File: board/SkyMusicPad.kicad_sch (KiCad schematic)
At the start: 32 parts, among them SW1 RotaryEncoder_Switch

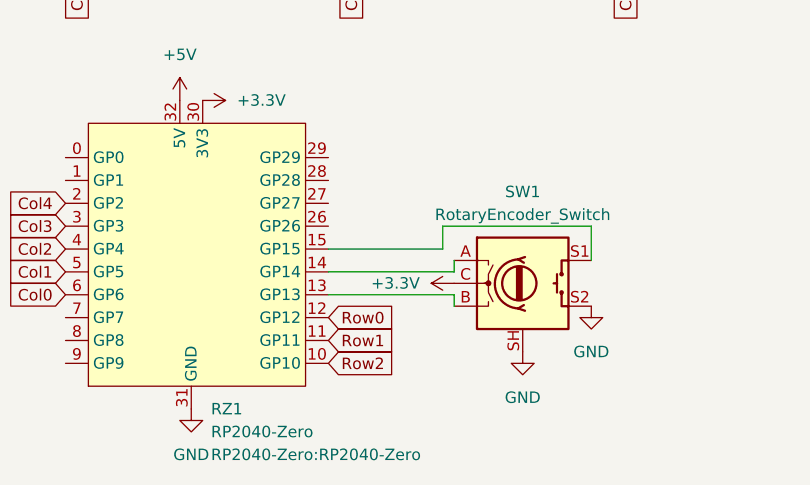
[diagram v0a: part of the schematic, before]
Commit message: Adjusted rotary encoder to have common point GND
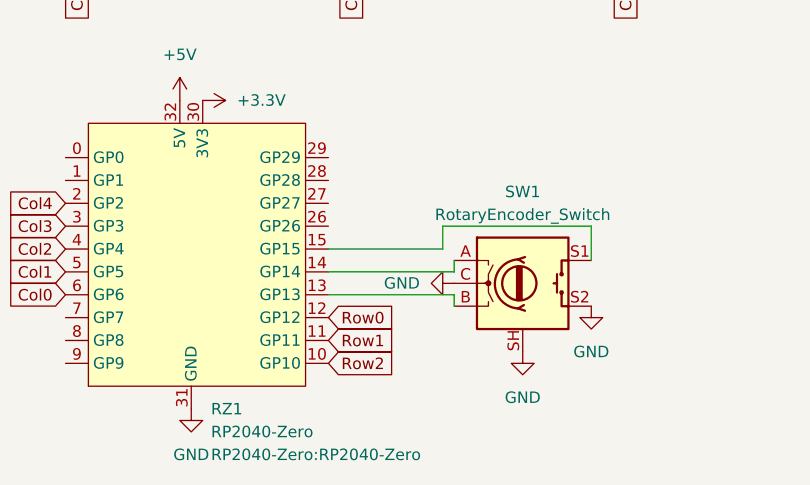
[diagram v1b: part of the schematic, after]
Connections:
- net +3.3V: no longer SW1.C
- net GND: now also SW1.C
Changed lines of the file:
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@@
+    )
+  )
+  (symbol (lib_id "power:GND") (at 191.77 120.65 270) (unit 1)
+    (in_bom yes) (on_board yes) (dnp no) (fields_autoplaced)
+    (property "Reference" "#PWR04" (at 185.42 120.65 0)
+      (effects (font (size 1.27 1.27)) hide)
+    )
+    (property "Value" "GND" (at 187.96 120.65 90)
+      (effects (font (size 1.27 1.27)) (justify right))
+    )
+    (property "Footprint" "" (at 191.77 120.65 0)
+      (effects (font (size 1.27 1.27)) hide)
+    )
+    (property "Datasheet" "" (at 191.77 120.65 0)
+      (effects (font (size 1.27 1.27)) hide)
+    )
+    (pin "1")
+    (instances
+      (project "SkyMusicPad"
+        (path "/892c3dfc-ea33-45ad-8367-abbb3e31e120"
+          (reference "#PWR04") (unit 1)
+        )
+      )
     )
   )
@@
         )
       )
-    )
-  )
-  (symbol (lib_id "power:+3.3V") (at 191.77 120.65 90) (unit 1)
-    (in_bom yes) (on_board yes) (dnp no) (fields_autoplaced)
-    (property "Reference" "#PWR04" (at 195.58 120.65 0)
-      (effects (font (size 1.27 1.27)) hide)
-    )
-    (property "Value" "+3.3V" (at 187.96 120.65 90)
-      (effects (font (size 1.27 1.27)) (justify left))
-    )
-    (property "Footprint" "" (at 191.77 120.65 0)
-      (effects (font (size 1.27 1.27)) hide)
-    )
-    (property "Datasheet" "" (at 191.77 120.65 0)
-      (effects (font (size 1.27 1.27)) hide)
-    )
-    (pin "1")
-    (instances
-      (project "SkyMusicPad"
-        (path "/892c3dfc-ea33-45ad-8367-abbb3e31e120"
-          (reference "#PWR04") (unit 1)
-        )
-      )

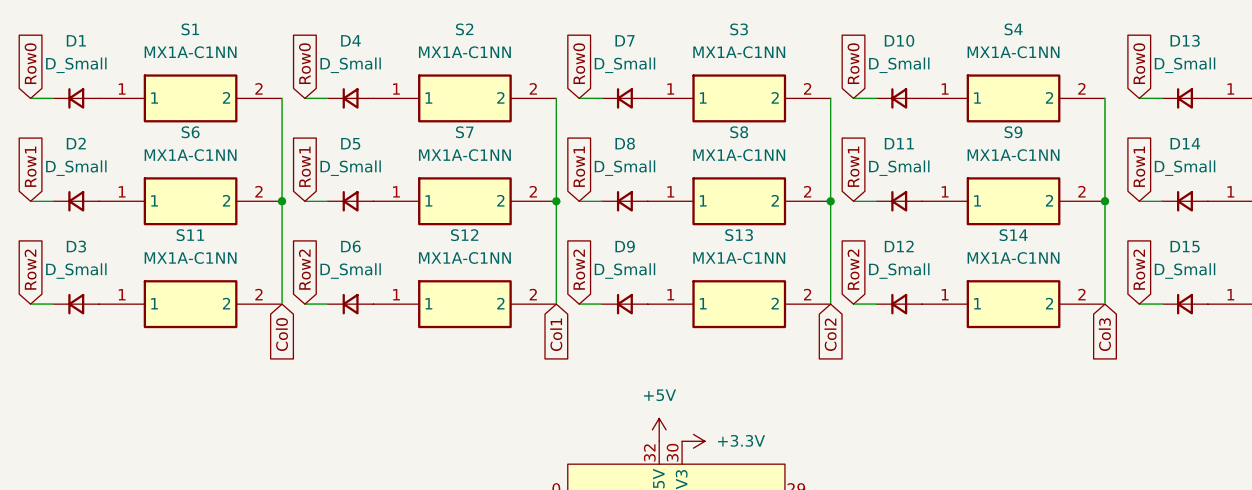
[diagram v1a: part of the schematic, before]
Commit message: Fixed the use of the incorrect footprint for MX
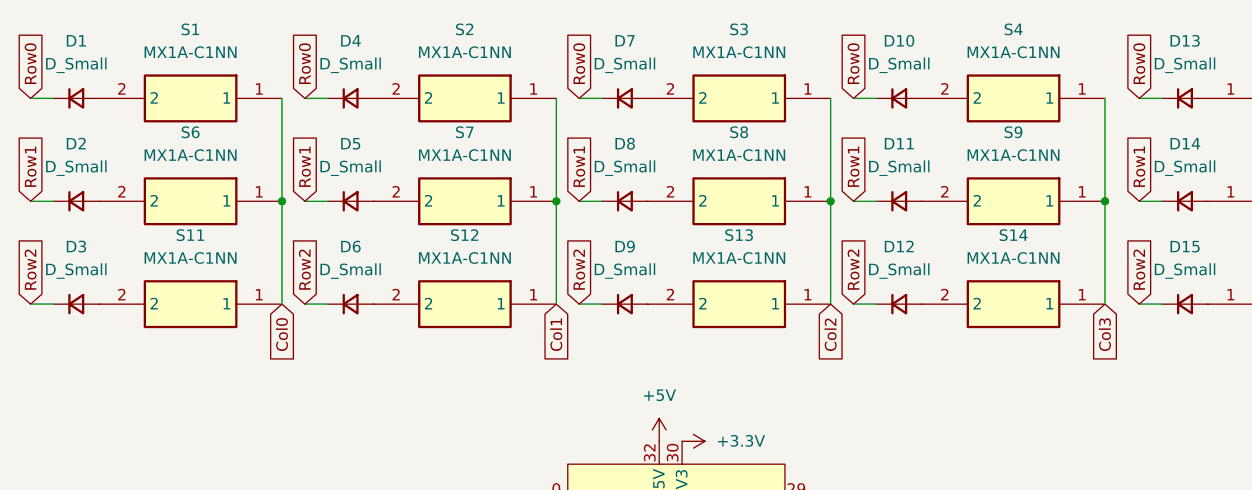
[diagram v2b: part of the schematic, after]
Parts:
- S1, S10, S11, S12, S13, S14, S15, S2, S3, S4, S5, S6, S7, S8, S9: footprint MX1A-C1NN:MX1AC1NN -> Button_Switch_Keyboard:SW_Cherry_MX_1.00u_PCB
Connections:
- net Col0: now also S1.1, S11.1, S6.1; no longer S1.2, S11.2, S6.2
- net Col1: now also S12.1, S2.1, S7.1; no longer S12.2, S2.2, S7.2
- net Col2: now also S13.1, S3.1, S8.1; no longer S13.2, S3.2, S8.2
- net Col3: now also S14.1, S4.1, S9.1; no longer S14.2, S4.2, S9.2
- net at D6.2 (A): now also S12.2; no longer S12.1
- net at D12.2 (A): now also S14.2; no longer S14.1
- net at D9.2 (A): now also S13.2; no longer S13.1
- net at D2.2 (A): now also S6.2; no longer S6.1
- net at D1.2 (A): now also S1.2; no longer S1.1
- net at D3.2 (A): now also S11.2; no longer S11.1
- net at D11.2 (A): now also S9.2; no longer S9.1
- net at D4.2 (A): now also S2.2; no longer S2.1
- net at D8.2 (A): now also S8.2; no longer S8.1
- net at D10.2 (A): now also S4.2; no longer S4.1
- net at D7.2 (A): now also S3.2; no longer S3.1
- net at D5.2 (A): now also S7.2; no longer S7.1

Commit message: a
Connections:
- net Col4: now also S10.1, S15.1, S5.1; no longer S10.2, S15.2, S5.2
- net at D14.2 (A): now also S10.2; no longer S10.1
- net at D15.2 (A): now also S15.2; no longer S15.1
- net at D13.2 (A): now also S5.2; no longer S5.1
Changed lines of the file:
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@@
 (kicad_sch (version 20230121) (generator eeschema)
   (paper "A4")
+  (junction (at 242.57 73.66) (diameter 0) (color 0 0 0 0)
+  )
   (junction (at 149.86 73.66) (diameter 0) (color 0 0 0 0)
   )
-  (junction (at 242.57 73.66) (diameter 0) (color 0 0 0 0)
-  )
   (junction (at 210.82 73.66) (diameter 0) (color 0 0 0 0)
   )
@@
     (stroke (width 0) (type default))
   )
+  (wire (pts (xy 152.4 85.09) (xy 154.94 85.09))
+    (stroke (width 0) (type default))
+  )
   (wire (pts (xy 242.57 73.66) (xy 242.57 85.09))
-    (stroke (width 0) (type default))
-  )
-  (wire (pts (xy 152.4 85.09) (xy 154.94 85.09))
     (stroke (width 0) (type default))
   )
@@
     )
   )
-  (symbol (lib_id "MX1A-C1NN:MX1A-C1NN") (at 222.25 62.23 0) (unit 1)
-    (in_bom yes) (on_board yes) (dnp no) (fields_autoplaced)
+  (symbol (lib_id "MX1A-C1NN:MX1A-C1NN") (at 242.57 62.23 0) (mirror y) (unit 1)
+    (in_bom yes) (on_board yes) (dnp no)
     (property "Reference" "S5" (at 232.41 54.61 0)
       (effects (font (size 1.27 1.27)))
@@
       (effects (font (size 1.27 1.27)))
     )
-    (property "Footprint" "Button_Switch_Keyboard:SW_Cherry_MX_1.00u_PCB" (at 238.76 157.15 0)
-      (effects (font (size 1.27 1.27)) (justify left top) hide)
-    )
-    (property "Datasheet" "https://media.digikey.com/pdf/Data%20Sheets/Cherry%20PDFs/MX%20Series.pdf" (at 238.76 257.15 0)
-      (effects (font (size 1.27 1.27)) (justify left top) hide)
-    )
-    (property "Height" "15.2" (at 238.76 457.15 0)
-      (effects (font (size 1.27 1.27)) (justify left top) hide)
-    )
-    (property "Mouser Part Number" "540-MX1A-C1NN" (at 238.76 557.15 0)
-      (effects (font (size 1.27 1.27)) (justify left top) hide)
-    )
-    (property "Mouser Price/Stock" "https://www.mouser.co.uk/ProductDetail/CHERRY/MX1A-C1NN?qs=Z9t1pRjfOcwvorA009Lo0w%3D%3D" (at 238.76 657.15 0)
-      (effects (font (size 1.27 1.27)) (justify left top) hide)
-    )
-    (property "Manufacturer_Name" "Cherry" (at 238.76 757.15 0)
-      (effects (font (size 1.27 1.27)) (justify left top) hide)
-    )
-    (property "Manufacturer_Part_Number" "MX1A-C1NN" (at 238.76 857.15 0)
+    (property "Footprint" "Button_Switch_Keyboard:SW_Cherry_MX_1.00u_PCB" (at 226.06 157.15 0)
+      (effects (font (size 1.27 1.27)) (justify left top) hide)
+    )
+    (property "Datasheet" "https://media.digikey.com/pdf/Data%20Sheets/Cherry%20PDFs/MX%20Series.pdf" (at 226.06 257.15 0)
+      (effects (font (size 1.27 1.27)) (justify left top) hide)
+    )
+    (property "Height" "15.2" (at 226.06 457.15 0)
+      (effects (font (size 1.27 1.27)) (justify left top) hide)
+    )
+    (property "Mouser Part Number" "540-MX1A-C1NN" (at 226.06 557.15 0)
+      (effects (font (size 1.27 1.27)) (justify left top) hide)
+    )
+    (property "Mouser Price/Stock" "https://www.mouser.co.uk/ProductDetail/CHERRY/MX1A-C1NN?qs=Z9t1pRjfOcwvorA009Lo0w%3D%3D" (at 226.06 657.15 0)
+      (effects (font (size 1.27 1.27)) (justify left top) hide)
+    )
+    (property "Manufacturer_Name" "Cherry" (at 226.06 757.15 0)
+      (effects (font (size 1.27 1.27)) (justify left top) hide)
+    )
+    (property "Manufacturer_Part_Number" "MX1A-C1NN" (at 226.06 857.15 0)
       (effects (font (size 1.27 1.27)) (justify left top) hide)
     )
@@
     )
   )
-  (symbol (lib_id "MX1A-C1NN:MX1A-C1NN") (at 222.25 73.66 0) (unit 1)
-    (in_bom yes) (on_board yes) (dnp no) (fields_autoplaced)
+  (symbol (lib_id "MX1A-C1NN:MX1A-C1NN") (at 242.57 73.66 0) (mirror y) (unit 1)
+    (in_bom yes) (on_board yes) (dnp no)
     (property "Reference" "S10" (at 232.41 66.04 0)
       (effects (font (size 1.27 1.27)))
@@
       (effects (font (size 1.27 1.27)))
     )
-    (property "Footprint" "Button_Switch_Keyboard:SW_Cherry_MX_1.00u_PCB" (at 238.76 168.58 0)
-      (effects (font (size 1.27 1.27)) (justify left top) hide)
-    )
-    (property "Datasheet" "https://media.digikey.com/pdf/Data%20Sheets/Cherry%20PDFs/MX%20Series.pdf" (at 238.76 268.58 0)
-      (effects (font (size 1.27 1.27)) (justify left top) hide)
-    )
-    (property "Height" "15.2" (at 238.76 468.58 0)
-      (effects (font (size 1.27 1.27)) (justify left top) hide)
-    )
-    (property "Mouser Part Number" "540-MX1A-C1NN" (at 238.76 568.58 0)
-      (effects (font (size 1.27 1.27)) (justify left top) hide)
-    )
-    (property "Mouser Price/Stock" "https://www.mouser.co.uk/ProductDetail/CHERRY/MX1A-C1NN?qs=Z9t1pRjfOcwvorA009Lo0w%3D%3D" (at 238.76 668.58 0)
-      (effects (font (size 1.27 1.27)) (justify left top) hide)
-    )
-    (property "Manufacturer_Name" "Cherry" (at 238.76 768.58 0)
-      (effects (font (size 1.27 1.27)) (justify left top) hide)
-    )
-    (property "Manufacturer_Part_Number" "MX1A-C1NN" (at 238.76 868.58 0)
+    (property "Footprint" "Button_Switch_Keyboard:SW_Cherry_MX_1.00u_PCB" (at 226.06 168.58 0)
+      (effects (font (size 1.27 1.27)) (justify left top) hide)
+    )
+    (property "Datasheet" "https://media.digikey.com/pdf/Data%20Sheets/Cherry%20PDFs/MX%20Series.pdf" (at 226.06 268.58 0)
+      (effects (font (size 1.27 1.27)) (justify left top) hide)
+    )
+    (property "Height" "15.2" (at 226.06 468.58 0)
+      (effects (font (size 1.27 1.27)) (justify left top) hide)
+    )
+    (property "Mouser Part Number" "540-MX1A-C1NN" (at 226.06 568.58 0)
+      (effects (font (size 1.27 1.27)) (justify left top) hide)
+    )
+    (property "Mouser Price/Stock" "https://www.mouser.co.uk/ProductDetail/CHERRY/MX1A-C1NN?qs=Z9t1pRjfOcwvorA009Lo0w%3D%3D" (at 226.06 668.58 0)
+      (effects (font (size 1.27 1.27)) (justify left top) hide)
+    )
+    (property "Manufacturer_Name" "Cherry" (at 226.06 768.58 0)
+      (effects (font (size 1.27 1.27)) (justify left top) hide)
+    )
+    (property "Manufacturer_Part_Number" "MX1A-C1NN" (at 226.06 868.58 0)
       (effects (font (size 1.27 1.27)) (justify left top) hide)
     )
@@
     )
   )
-  (symbol (lib_id "MX1A-C1NN:MX1A-C1NN") (at 222.25 85.09 0) (unit 1)
-    (in_bom yes) (on_board yes) (dnp no) (fields_autoplaced)
+  (symbol (lib_id "MX1A-C1NN:MX1A-C1NN") (at 242.57 85.09 0) (mirror y) (unit 1)
+    (in_bom yes) (on_board yes) (dnp no)
     (property "Reference" "S15" (at 232.41 77.47 0)
       (effects (font (size 1.27 1.27)))
@@
       (effects (font (size 1.27 1.27)))
     )
-    (property "Footprint" "Button_Switch_Keyboard:SW_Cherry_MX_1.00u_PCB" (at 238.76 180.01 0)
-      (effects (font (size 1.27 1.27)) (justify left top) hide)
-    )
-    (property "Datasheet" "https://media.digikey.com/pdf/Data%20Sheets/Cherry%20PDFs/MX%20Series.pdf" (at 238.76 280.01 0)
-      (effects (font (size 1.27 1.27)) (justify left top) hide)
-    )
-    (property "Height" "15.2" (at 238.76 480.01 0)
-      (effects (font (size 1.27 1.27)) (justify left top) hide)
-    )
-    (property "Mouser Part Number" "540-MX1A-C1NN" (at 238.76 580.01 0)
-      (effects (font (size 1.27 1.27)) (justify left top) hide)
-    )
-    (property "Mouser Price/Stock" "https://www.mouser.co.uk/ProductDetail/CHERRY/MX1A-C1NN?qs=Z9t1pRjfOcwvorA009Lo0w%3D%3D" (at 238.76 680.01 0)
-      (effects (font (size 1.27 1.27)) (justify left top) hide)
-    )
-    (property "Manufacturer_Name" "Cherry" (at 238.76 780.01 0)
-      (effects (font (size 1.27 1.27)) (justify left top) hide)
-    )
-    (property "Manufacturer_Part_Number" "MX1A-C1NN" (at 238.76 880.01 0)
-      (effects (font (size 1.27 1.27)) (justify left top) hide)
-    )
+    (property "Footprint" "Button_Switch_Keyboard:SW_Cherry_MX_1.00u_PCB" (at 226.06 180.01 0)
+      (effects (font (size 1.27 1.27)) (justify left top) hide)
+    )
+    (property "Datasheet" "https://media.digikey.com/pdf/Data%20Sheets/Cherry%20PDFs/MX%20Series.pdf" (at 226.06 280.01 0)
+      (effects (font (size 1.27 1.27)) (justify left top) hide)
+    )
+    (property "Height" "15.2" (at 226.06 480.01 0)
+      (effects (font (size 1.27 1.27)) (justify left top) hide)
+    )
+    (property "Mouser Part Number" "540-MX1A-C1NN" (at 226.06 580.01 0)
+      (effects (font (size 1.27 1.27)) (justify left top) hide)
+    )
+    (property "Mouser Price/Stock" "https://www.mouser.co.uk/ProductDetail/CHERRY/MX1A-C1NN?qs=Z9t1pRjfOcwvorA009Lo0w%3D%3D" (at 226.06 680.01 0)
+      (effects (font (size 1.27 1.27)) (justify left top) hide)
+    )
+    (property "Manufacturer_Name" "Cherry" (at 226.06 780.01 0)
+      (effects (font (size 1.27 1.27)) (justify left top) hide)
+    )
+    (property "Manufacturer_Part_Number" "MX1A-C1NN" (at 226.06 880.01 0)
+      (effects (font (size 1.27 1.27)) (justify left top) hide)
+    )

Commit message: misc changes
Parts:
- removed RZ1: RP2040-Zero, RP2040-Zero:RP2040-Zero, symbol rp2040-zero:RP2040-Zero
- added C1, C10, C11, C12, C2, C4, C6, C7, C8, C9: 100n, Capacitor_SMD:C_0402_1005Metric, symbol Device:C
- added C13, C14: 27p, Capacitor_SMD:C_0402_1005Metric, symbol Device:C
- added C15, C16, C17: 10u, Capacitor_SMD:C_0805_2012Metric, symbol Device:C
- added C3, C5: 1u, Capacitor_SMD:C_0402_1005Metric, symbol Device:C
- added J1: USB_C_Receptacle_USB2.0, Connector_USB:USB_C_Receptacle_Amphenol_12401548E4-2A, symbol Connector:USB_C_Receptacle_USB2.0
- added R1, R2: 27, Capacitor_SMD:C_0402_1005Metric, symbol Device:R
- added R3, R5: 1k, Capacitor_SMD:C_0402_1005Metric, symbol Device:R
- added R4: DNF, Capacitor_SMD:C_0402_1005Metric, symbol Device:R
- added R6, R7: 5.1k, Capacitor_SMD:C_0402_1005Metric, symbol Device:R
- added SW2: SW_Push, symbol Switch:SW_Push
- added U1: RP2040, Package_DFN_QFN:QFN-56-1EP_7x7mm_P0.4mm_EP3.2x3.2mm, symbol MCU_RaspberryPi:RP2040
- added U2: W25Q128JVS, Package_SO:SOIC-8_5.23x5.23mm_P1.27mm, symbol Memory_Flash:W25Q128JVS
- added U3: NCP1117-3.3_SOT223, Package_TO_SOT_SMD:SOT-223-3_TabPin2, symbol Regulator_Linear:NCP1117-3.3_SOT223
- added Y1: ABLS-12.000MHZ-B4-T, RP2040_minimal:Crystal_SMD_HC49-US, symbol Device:Crystal
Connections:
- net +3.3V: now also C10.1, C11.1, C12.1, C15.1, C17.1, C4.1, C5.1, C6.1, C7.1, C8.1, C9.1, R4.1, U1.1 (IOVDD), U1.10 (IOVDD), U1.22 (IOVDD), U1.33 (IOVDD), U1.42 (IOVDD), U1.43 (ADC_AVDD), U1.44 (VREG_IN), U1.48 (USB_VDD), U1.49 (IOVDD), U2.8 (VCC), U3.2 (VO)
- net +5V: now also C16.1, J1.A4 (VBUS), J1.A9 (VBUS), J1.B4 (VBUS), J1.B9 (VBUS), U3.3 (VI)
- net Col0: now also U1.8 (GPIO6)
- net Col1: now also U1.7 (GPIO5)
- net Col2: now also U1.6 (GPIO4)
- net Col3: now also U1.5 (GPIO3)
- net Col4: now also U1.4 (GPIO2)
- net GND: now also C1.2, C10.2, C11.2, C12.2, C13.2, C14.2, C15.2, C16.2, C17.2, C2.2, C3.2, C4.2, C5.2, C6.2, C7.2, C8.2, C9.2, J1.A1 (GND), J1.A12 (GND), J1.B1 (GND), J1.B12 (GND), J1.S1 (SHIELD), R6.1, R7.1, SW2.1, U1.19 (TESTEN), U1.57 (GND), U2.4 (GND), U3.1 (GND)
- net Row0: now also U1.18 (GPIO15)
- net Row1: now also U1.17 (GPIO14)
- net Row2: now also U1.16 (GPIO13)
- net GPIO18: now reaches SW1.A
- net GPIO18: now also U1.29 (GPIO18)
- net GPIO20: now reaches SW1.B
- net GPIO20: now also U1.31 (GPIO20)
- net GPIO16: now reaches SW1.S1
- net GPIO16: now also U1.27 (GPIO16)
- new net: J1.B5 (CC2), R7.2
- new net: J1.A5 (CC1), R6.2
- new net: C14.1, R5.2, Y1.2
- new net +1V1: C1.1, C2.1, C3.1, U1.23 (DVDD), U1.45 (VREG_VOUT), U1.50 (DVDD)
- new net GPIO0: U1.2 (GPIO0)
- new net GPIO1: U1.3 (GPIO1)
- new net GPIO10: U1.13 (GPIO10)
- new net GPIO11: U1.14 (GPIO11)
- new net GPIO12: U1.15 (GPIO12)
- new net GPIO17: U1.28 (GPIO17)
- new net GPIO19: U1.30 (GPIO19)
- new net GPIO21: U1.32 (GPIO21)
- new net GPIO22: U1.34 (GPIO22)
- new net GPIO23: U1.35 (GPIO23)
- new net GPIO24: U1.36 (GPIO24)
- new net GPIO25: U1.37 (GPIO25)
- new net GPIO26_ADC0: U1.38 (GPIO26_ADC0)
- new net GPIO27_ADC1: U1.39 (GPIO27_ADC1)
- new net GPIO28_ADC2: U1.40 (GPIO28_ADC2)
- new net GPIO29_ADC3: U1.41 (GPIO29_ADC3)
- new net GPIO7: U1.9 (GPIO7)
- new net GPIO8: U1.11 (GPIO8)
- new net GPIO9: U1.12 (GPIO9)
- new net PICO_USB_D+: R1.2, U1.47 (USB_DP)
- new net PICO_USB_D-: R2.2, U1.46 (USB_DM)
- new net QSPI_SCLK: U1.52 (QSPI_SCLK), U2.6 (CLK)
- new net QSPI_SD0: U1.53 (QSPI_SD0), U2.5 (DI(IO0))
- new net QSPI_SD1: U1.55 (QSPI_SD1), U2.2 (DO(IO1))
- new net QSPI_SD2: U1.54 (QSPI_SD2), U2.3 (IO2)
- new net QSPI_SD3: U1.51 (QSPI_SD3), U2.7 (IO3)
- new net QSPI_SS: R3.1, R4.2, U1.56 (QSPI_SS), U2.1 (~{CS})
- new net RUN: U1.26 (RUN)
- new net SWCLK: U1.24 (SWCLK)
- new net SWD: U1.25 (SWD)
- new net USB_D+: J1.A6 (D+), J1.B6 (D+), R1.1
- new net USB_D-: J1.A7 (D-), J1.B7 (D-), R2.1
- new net XIN: C13.1, U1.20 (XIN), Y1.1
- new net XOUT: R5.1, U1.21 (XOUT)
- new net ~{USB_BOOT}: R3.2, SW2.2
- no-connect marks 0 -> 2
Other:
- note added: "Crystal"
- note added: "Flash"
- note added: "Make sure C10 is close to pin 44 of RP2040"
- note added: "Make sure C8 is close to pin 45 of RP2040"
- note added: "Make sure R3 and R4 are close to RP2040"
- note added: "Power"
- moved on the sheet: D1, D10, D11, D12, D13, D14, D15, D2, D3, D4, D5, D6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
